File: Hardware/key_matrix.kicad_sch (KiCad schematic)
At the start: 96 parts, among them SW1 F7, SW10 8, SW11 9, SW12 0, SW13 -/_, SW14 +/=, SW15 BS, SW16 PAGE_DOWN, SW17 Y, SW18 U, SW19 I, SW2 F8, SW20 O, SW21 P, SW22 [, SW23 ], SW24 \, SW25 H, SW26 B, SW27 Space, SW28 J, SW29 N, SW3 F9, SW30 R_ALT, SW31 K, SW32 M, SW33 R_WIN, SW34 L, SW35 ,, SW36 R_FCT, SW37 ;, SW38 ., SW39 R_CTRL, SW4 F10, SW40 ', SW41 /, SW42 ARROW_L, SW43 RET, SW44 R_SHIFT, SW45 ARROW_D, SW46 HOME, SW47 ARROW_U, SW48 ARROW_R, SW5 F11, SW6 F12, SW7 DEL, SW8 PAGE_UP, SW9 7

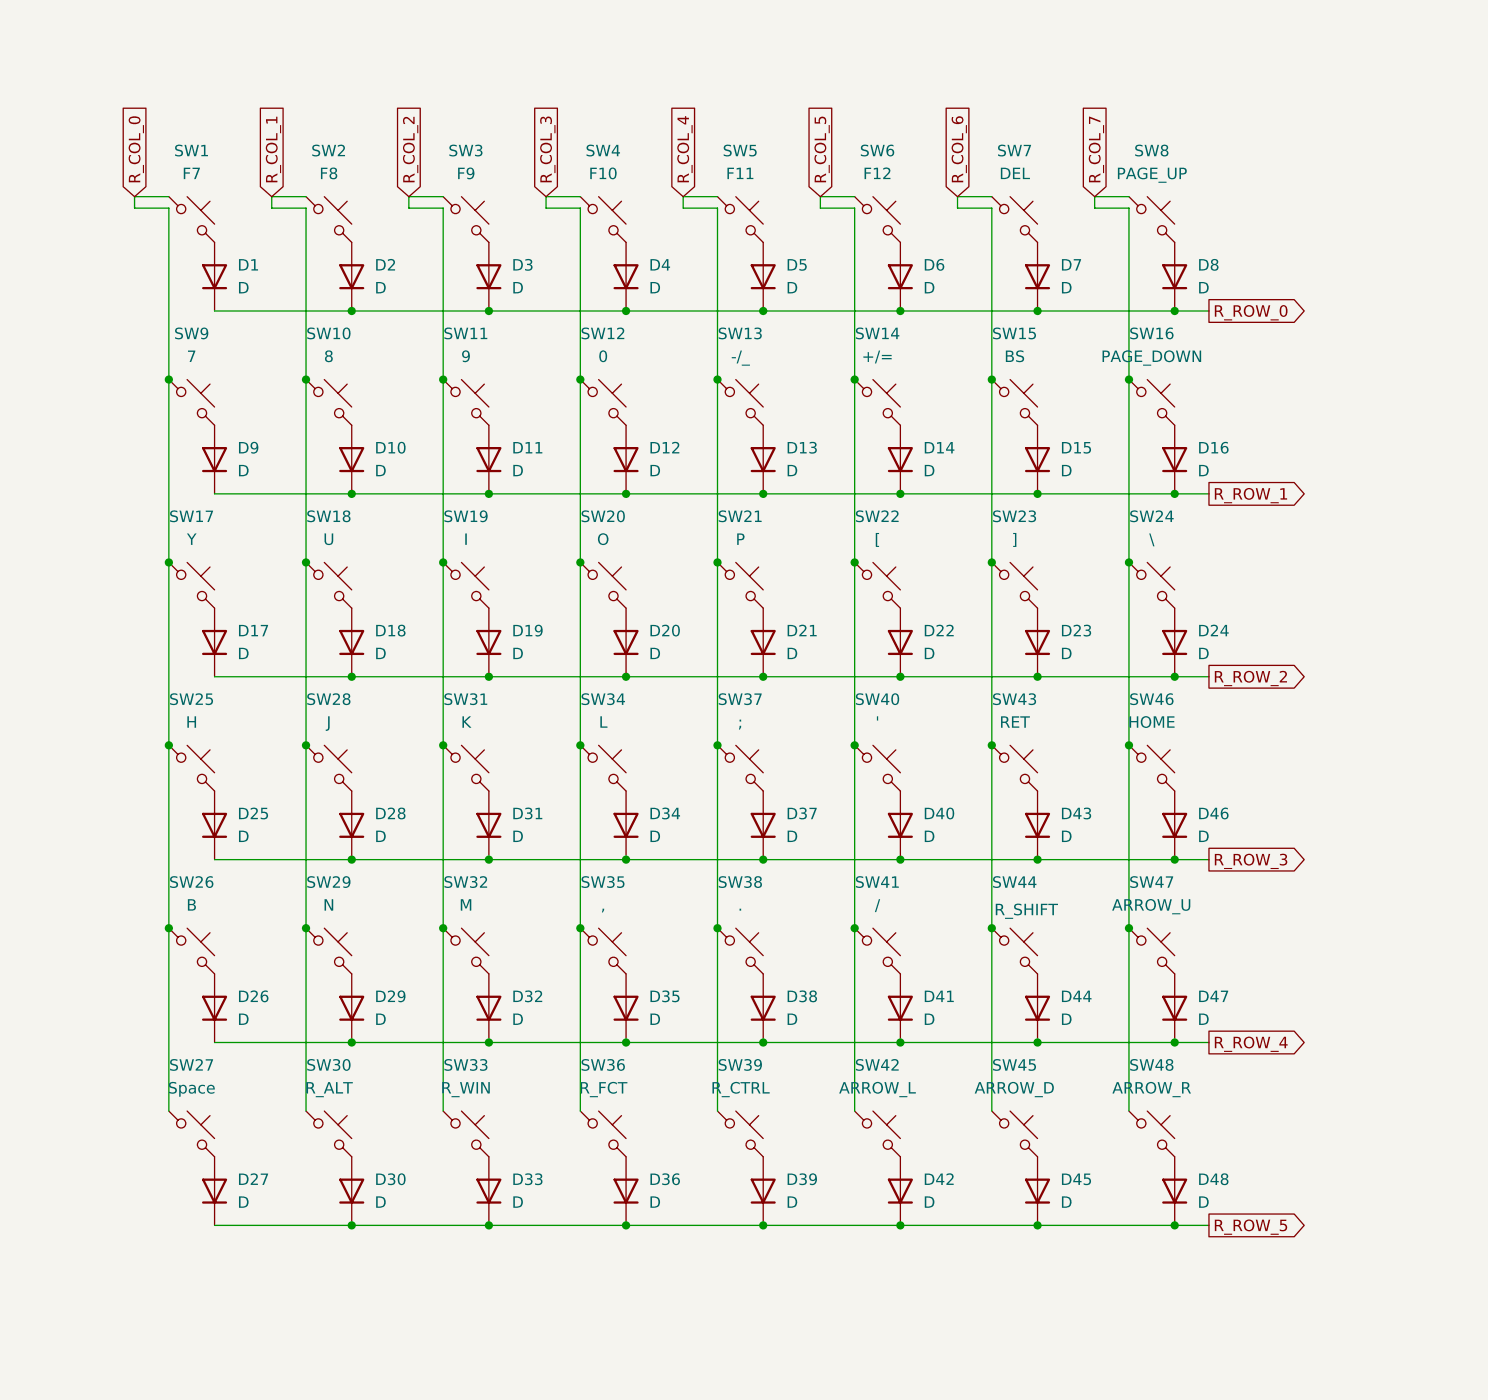
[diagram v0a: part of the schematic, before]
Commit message: Named all LHS keys
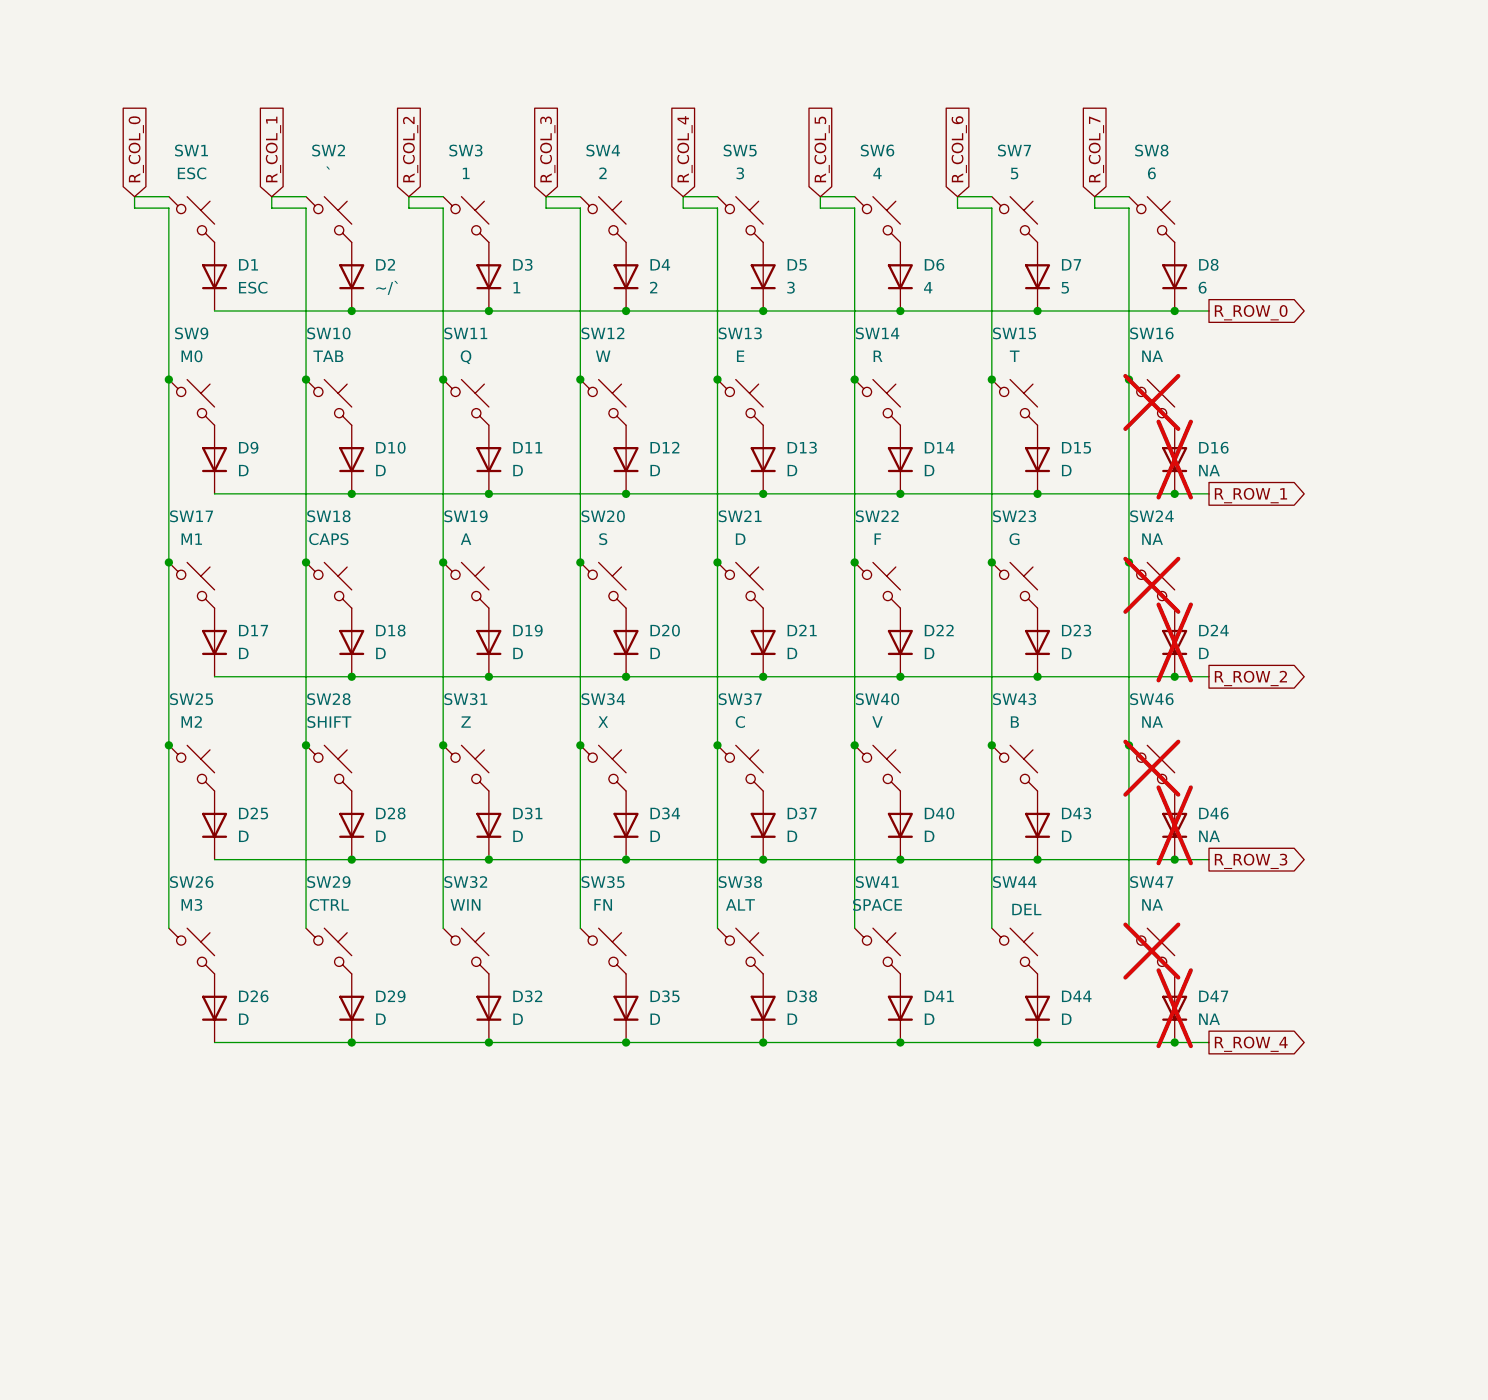
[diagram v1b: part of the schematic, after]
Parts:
- removed D27, D30, D33, D36, D39, D42, D45, D48: D, ScottoKeebs_Components:Diode_SOD-123, symbol Device:D
- removed SW27: Space, ScottoKeebs_Hotswap:Hotswap_MX_2.75u, symbol Switch:SW_Push_45deg
- removed SW30: R_ALT, symbol Switch:SW_Push_45deg
- removed SW33: R_WIN, symbol Switch:SW_Push_45deg
- removed SW36: R_FCT, symbol Switch:SW_Push_45deg
- removed SW39: R_CTRL, symbol Switch:SW_Push_45deg
- removed SW42: ARROW_L, symbol Switch:SW_Push_45deg
- removed SW45: ARROW_D, symbol Switch:SW_Push_45deg
- removed SW48: ARROW_R, symbol Switch:SW_Push_45deg
- D1: value D -> ESC
- D16, D46, D47: value D -> NA; now not fitted; now left out of the parts list
- D2: value D -> ~/`
- D24: now not fitted; now left out of the parts list
- D3: value D -> 1
- D4: value D -> 2
- D5: value D -> 3
- D6: value D -> 4
- D7: value D -> 5
- D8: value D -> 6
- SW1: value F7 -> ESC
- SW10: value 8 -> TAB
- SW11: value 9 -> Q
- SW12: value 0 -> W
- SW13: value -/_ -> E
- SW14: value +/= -> R
- SW15: value BS -> T
- SW16: value PAGE_DOWN -> NA; now not fitted; now left out of the parts list
- SW17: value Y -> M1
- SW18: value U -> CAPS
- SW19: value I -> A
- SW2: value F8 -> `
- SW20: value O -> S
- SW21: value P -> D
- SW22: value [ -> F
- SW23: value ] -> G
- SW24: value \ -> NA; now not fitted; now left out of the parts list
- SW25: value H -> M2
- SW26: value B -> M3
- SW28: value J -> SHIFT
- SW29: value N -> CTRL
- SW3: value F9 -> 1
- SW31: value K -> Z
- SW32: value M -> WIN
- SW34: value L -> X
- SW35: value , -> FN
- SW37: value ; -> C
- SW38: value . -> ALT
- SW4: value F10 -> 2
- SW40: value ' -> V
- SW41: value / -> SPACE
- SW43: value RET -> B
- SW44: value R_SHIFT -> DEL
- SW46: value HOME -> NA; now not fitted; now left out of the parts list
- SW47: value ARROW_U -> NA; now not fitted; now left out of the parts list
- SW5: value F11 -> 3
- SW6: value F12 -> 4
- SW7: value DEL -> 5
- SW8: value PAGE_UP -> 6
- SW9: value 7 -> M0

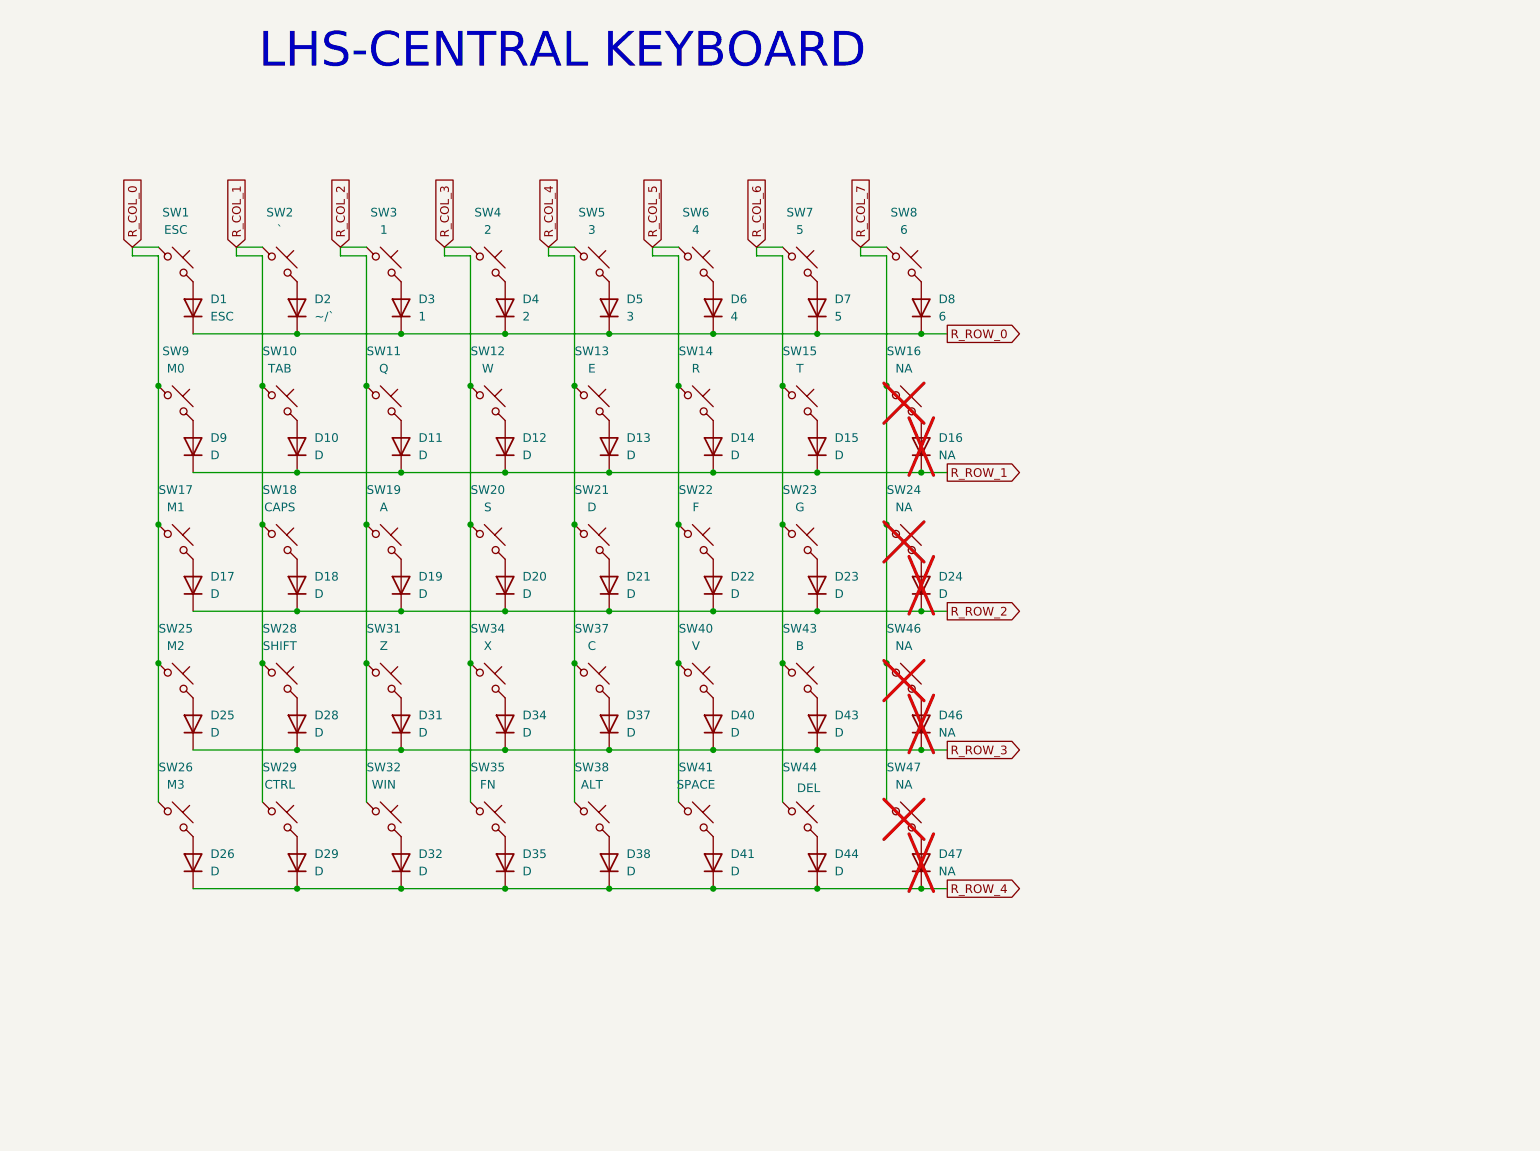
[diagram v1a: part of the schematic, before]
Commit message: Completed Final GUI Key Layout and PCB key layout draft
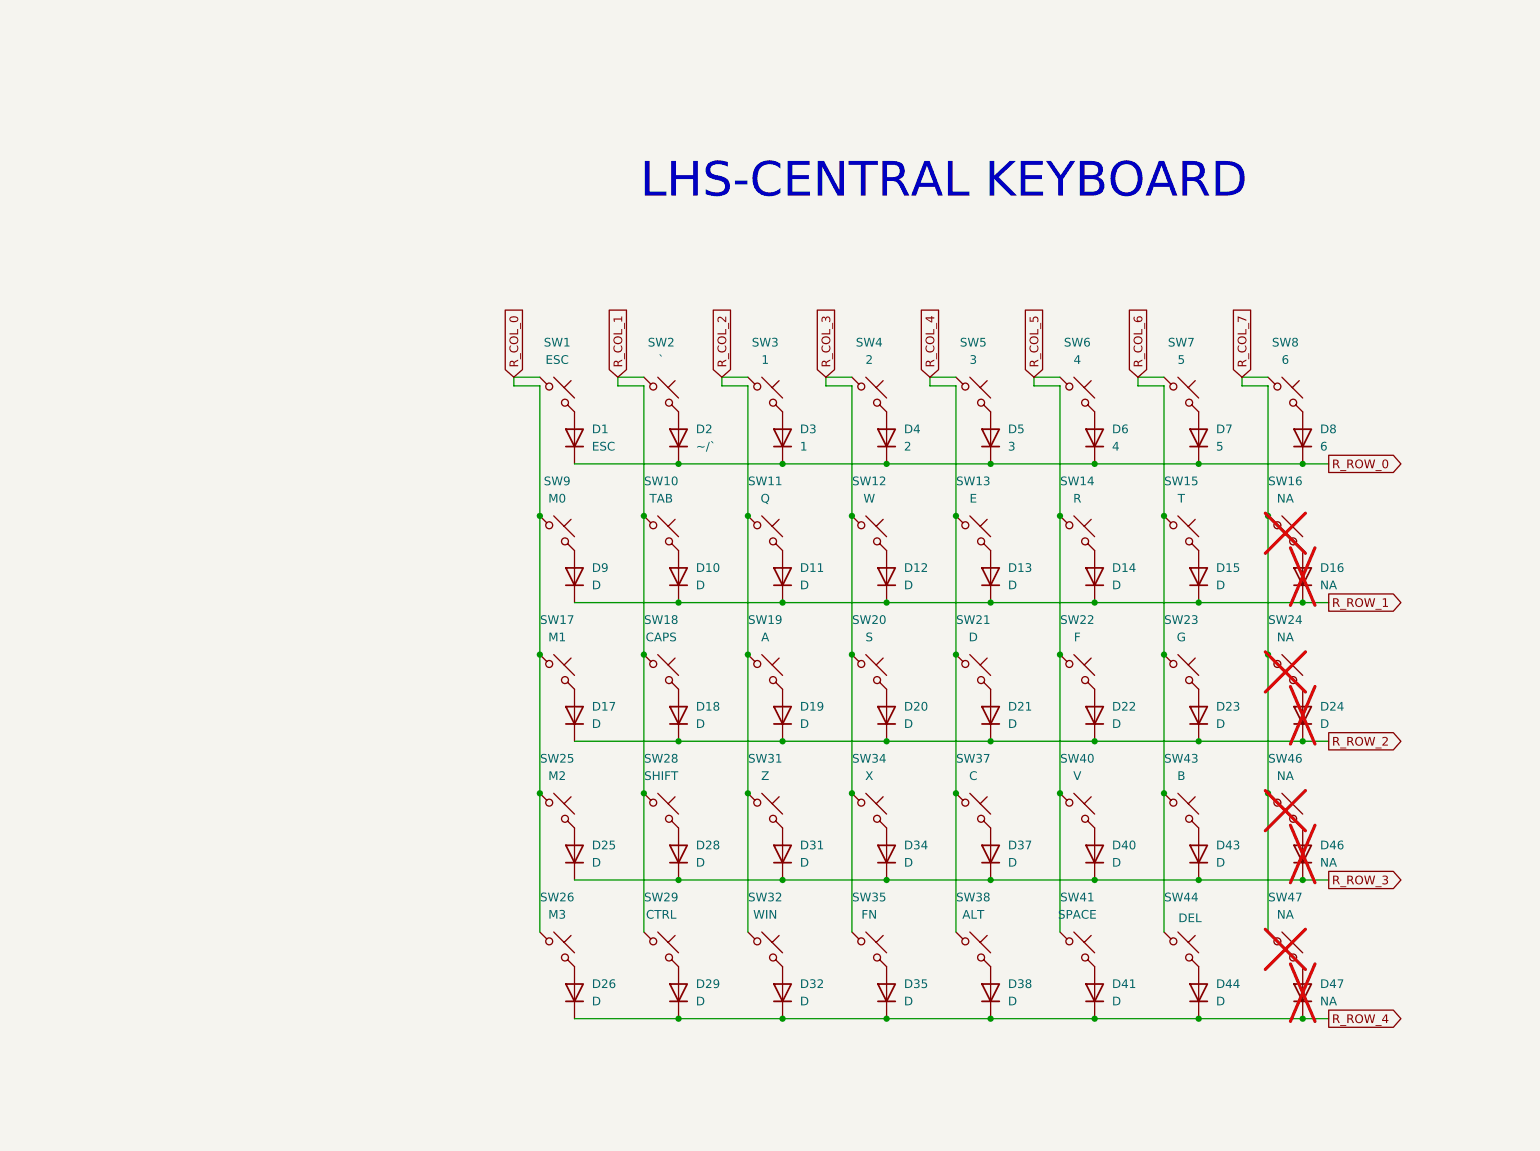
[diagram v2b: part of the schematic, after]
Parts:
- SW10: footprint ScottoKeebs_Hotswap:Hotswap_MX_1.00u -> ScottoKeebs_Hotswap:Hotswap_MX_1.50u
- SW18: footprint ScottoKeebs_Hotswap:Hotswap_MX_1.00u -> ScottoKeebs_Hotswap:Hotswap_MX_1.75u
- SW28: footprint ScottoKeebs_Hotswap:Hotswap_MX_1.00u -> ScottoKeebs_Hotswap:Hotswap_MX_2.25u
- SW29: footprint ScottoKeebs_Hotswap:Hotswap_MX_1.00u -> ScottoKeebs_Hotswap:Hotswap_MX_1.25u
- SW31, SW32, SW34, SW37, SW40, SW43, SW44: footprint (none) -> ScottoKeebs_Hotswap:Hotswap_MX_1.00u
- SW35, SW38: footprint (none) -> ScottoKeebs_Hotswap:Hotswap_MX_1.25u
- SW41: footprint (none) -> ScottoKeebs_Hotswap:Hotswap_MX_2.25u
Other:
- moved on the sheet: D1, D10, D11, D12, D13, D14, D15, D16, D17, D18, D19, D2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

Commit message: fix "T" key footprint
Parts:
- SW15: footprint ScottoKeebs_Hotswap:Hotswap_MX_2.00u -> ScottoKeebs_Hotswap:Hotswap_MX_1.00u
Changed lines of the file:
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@@
 			)
 		)
-		(property "Footprint" "ScottoKeebs_Hotswap:Hotswap_MX_2.00u"
+		(property "Footprint" "ScottoKeebs_Hotswap:Hotswap_MX_1.00u"
 			(at 298.45 96.52 0)
 			(effects
